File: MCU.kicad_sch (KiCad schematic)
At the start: 28 parts, among them J3 ADC_EXT_SUPPLY, U2 LPC55S28JBD100

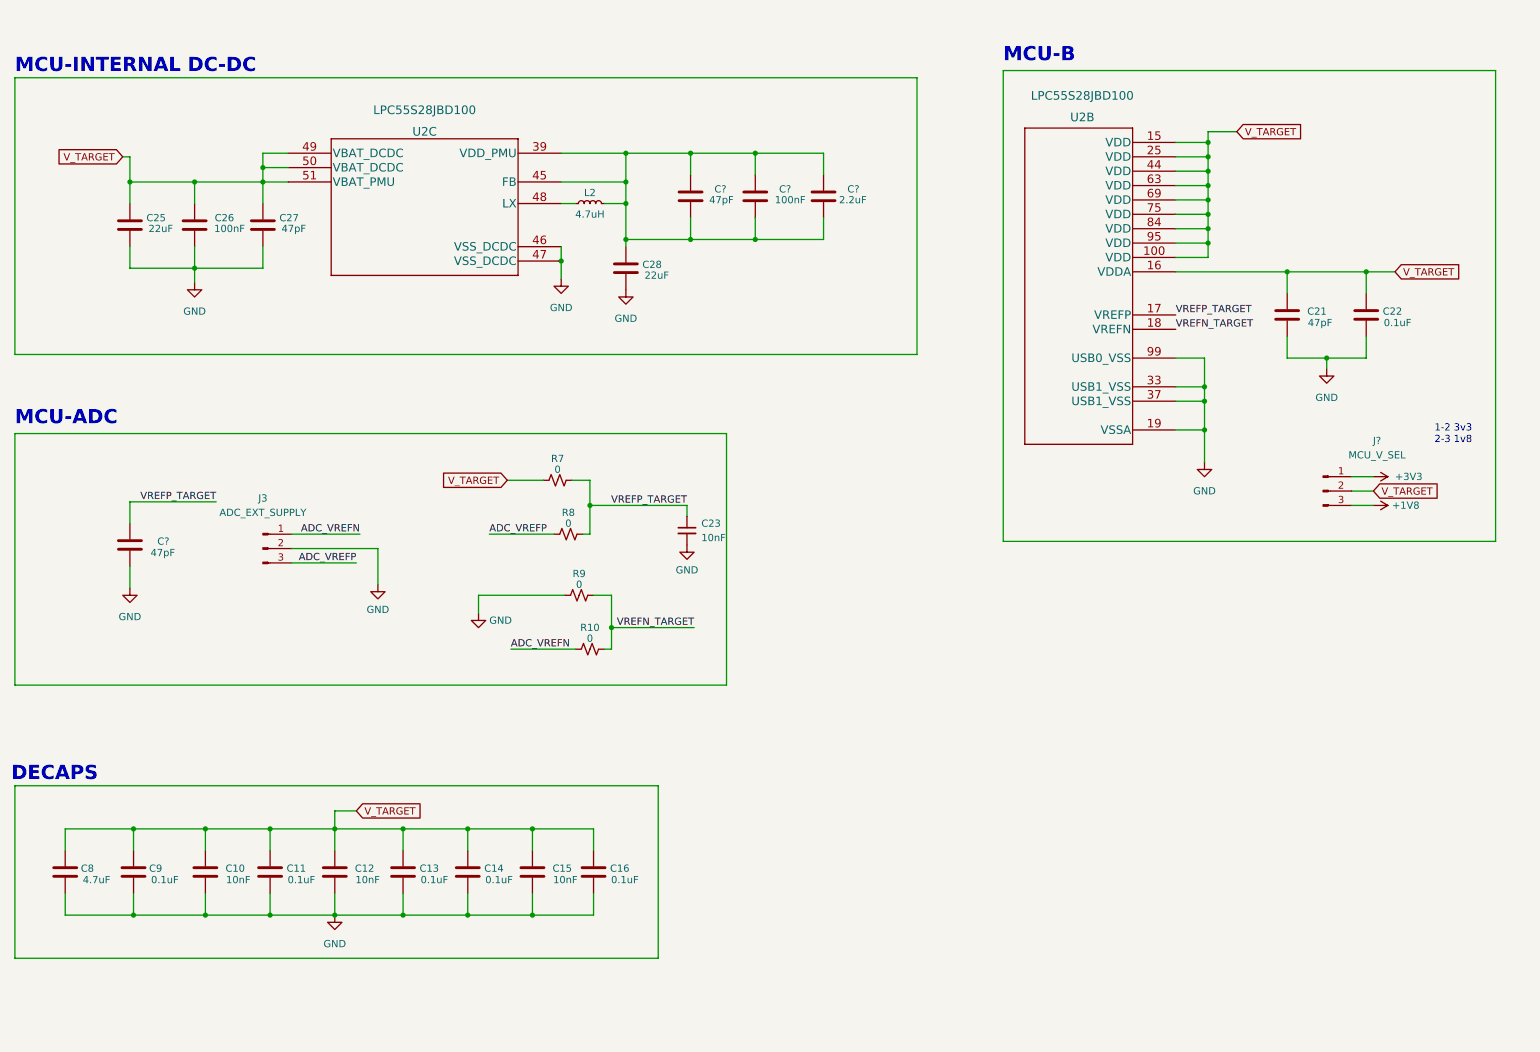
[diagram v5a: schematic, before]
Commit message: ISP Boot eklenecek
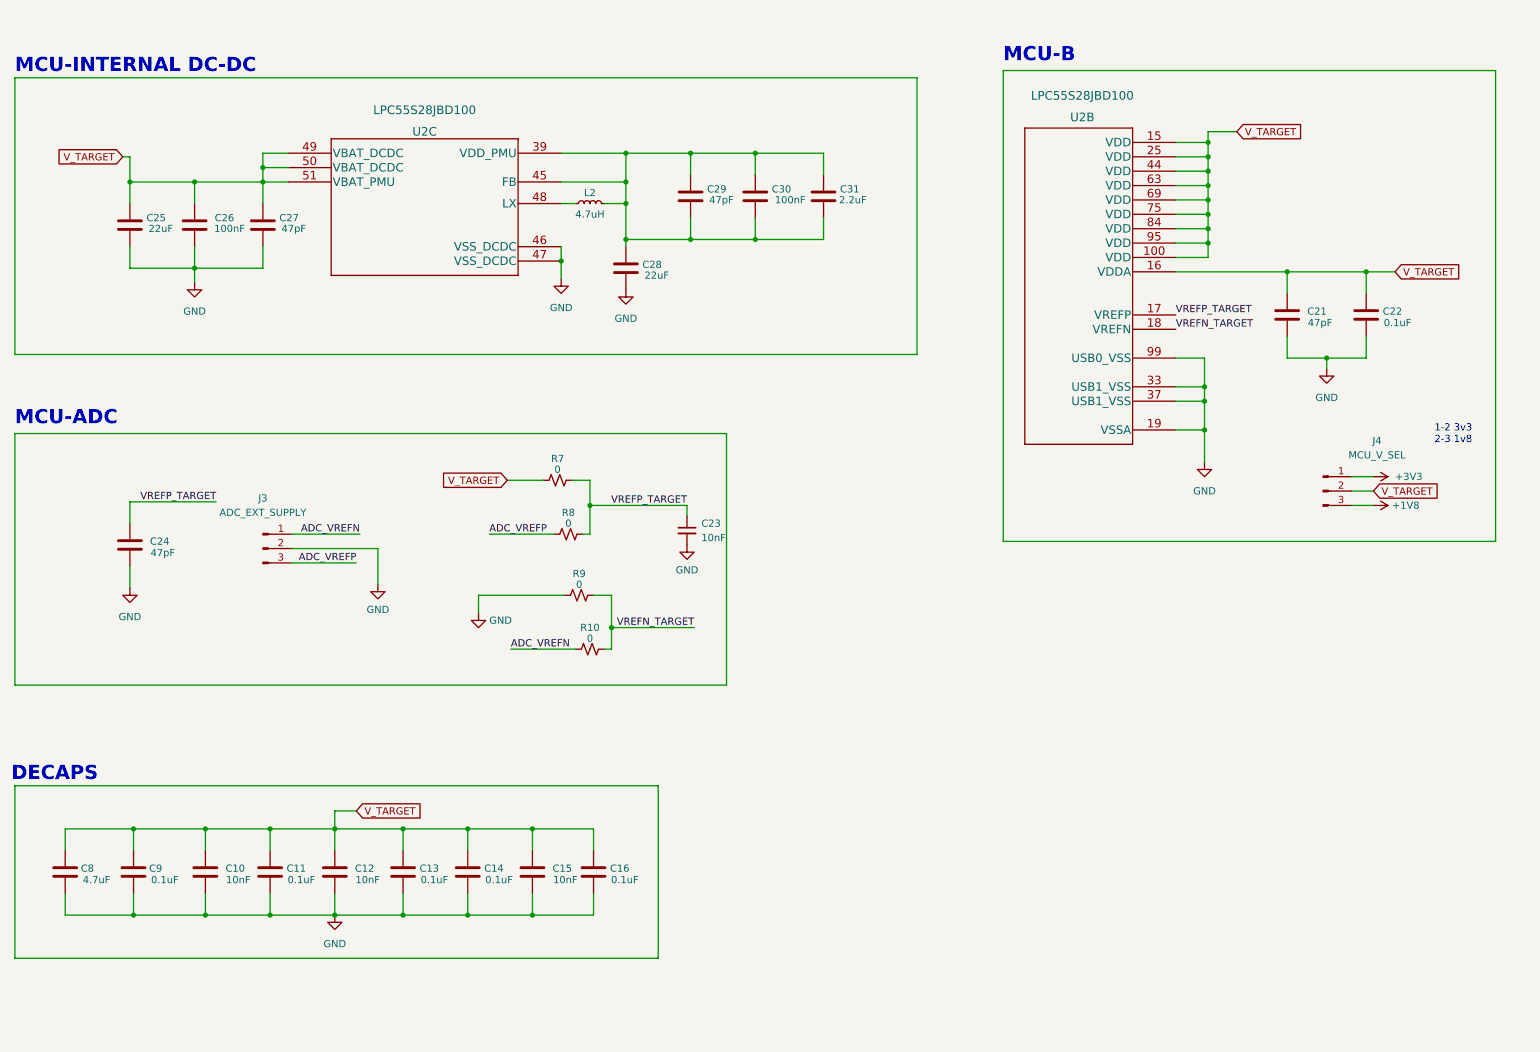
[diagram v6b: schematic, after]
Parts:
- C10, C11, C12, C13, C14, C15, C16, C21, C22, C25, C26, C27, C28, C8, C9: footprint Resistor_SMD:R_0603_1608Metric -> Capacitor_SMD:C_0603_1608Metric
- C23: footprint (none) -> Capacitor_SMD:C_0603_1608Metric
- C29, C30, C31: renamed from C?; footprint Resistor_SMD:R_0603_1608Metric -> Capacitor_SMD:C_0603_1608Metric
- U2: footprint HLQFP100 -> erkan-hw-lib:HLQFP100
- gave numbers to parts that had none: 2
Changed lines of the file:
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@@
       (effects (font (size 1.27 1.27)) (justify right))
     )
-    (property "Footprint" "Resistor_SMD:R_0603_1608Metric" (id 2) (at 78.4352 170.18 0)
+    (property "Footprint" "Capacitor_SMD:C_0603_1608Metric" (id 2) (at 78.4352 170.18 0)
       (effects (font (size 1.27 1.27)) hide)
     )
@@
       (effects (font (size 1.524 1.524)))
     )
-    (property "Footprint" "HLQFP100" (id 2) (at 122.555 30.734 0)
+    (property "Footprint" "erkan-hw-lib:HLQFP100" (id 2) (at 122.555 30.734 0)
       (effects (font (size 1.524 1.524)) hide)
     )
@@
   (symbol (lib_id "power:+1V8") (at 260.985 101.6 270) (unit 1)
     (in_bom yes) (on_board yes)
-    (property "Reference" "#PWR?" (id 0) (at 257.175 101.6 0)
+    (property "Reference" "#PWR0120" (id 0) (at 257.175 101.6 0)
       (effects (font (size 1.27 1.27)) hide)
     )
@@
       (effects (font (size 1.27 1.27)) (justify left))
     )
-    (property "Footprint" "" (id 2) (at 139.7 106.045 0)
+    (property "Footprint" "Capacitor_SMD:C_0603_1608Metric" (id 2) (at 139.7 106.045 0)
       (effects (font (size 1.27 1.27)) hide)
     )
@@
   (symbol (lib_id "Device:C") (at 163.83 46.99 0) (unit 1)
     (in_bom yes) (on_board yes)
-    (property "Reference" "C?" (id 0) (at 170.18 45.72 0)
+    (property "Reference" "C31" (id 0) (at 170.18 45.72 0)
       (effects (font (size 1.27 1.27)) (justify right))
     )
@@
       (effects (font (size 1.27 1.27)) (justify right))
     )
-    (property "Footprint" "Resistor_SMD:R_0603_1608Metric" (id 2) (at 164.7952 50.8 0)
+    (property "Footprint" "Capacitor_SMD:C_0603_1608Metric" (id 2) (at 164.7952 50.8 0)
       (effects (font (size 1.27 1.27)) hide)
     )
@@
   (symbol (lib_id "power:+3V3") (at 260.985 96.52 270) (unit 1)
     (in_bom yes) (on_board yes) (fields_autoplaced)
-    (property "Reference" "#PWR?" (id 0) (at 257.175 96.52 0)
+    (property "Reference" "#PWR0133" (id 0) (at 257.175 96.52 0)
       (effects (font (size 1.27 1.27)) hide)
     )
@@
   (symbol (lib_id "power:GND") (at 41.275 116.205 0) (unit 1)
     (in_bom yes) (on_board yes) (fields_autoplaced)
-    (property "Reference" "#PWR?" (id 0) (at 41.275 122.555 0)
+    (property "Reference" "#PWR0134" (id 0) (at 41.275 122.555 0)
       (effects (font (size 1.27 1.27)) hide)
     )
@@
       (effects (font (size 1.27 1.27)) (justify right))
     )
-    (property "Footprint" "Resistor_SMD:R_0603_1608Metric" (id 2) (at 42.8752 170.18 0)
+    (property "Footprint" "Capacitor_SMD:C_0603_1608Metric" (id 2) (at 42.8752 170.18 0)
       (effects (font (size 1.27 1.27)) hide)
     )
@@
   (symbol (lib_id "Device:C") (at 151.765 46.99 0) (unit 1)
     (in_bom yes) (on_board yes)
-    (property "Reference" "C?" (id 0) (at 158.115 45.72 0)
+    (property "Reference" "C30" (id 0) (at 158.115 45.72 0)
       (effects (font (size 1.27 1.27)) (justify right))
     )
@@
       (effects (font (size 1.27 1.27)) (justify right))
     )
-    (property "Footprint" "Resistor_SMD:R_0603_1608Metric" (id 2) (at 152.7302 50.8 0)
+    (property "Footprint" "Capacitor_SMD:C_0603_1608Metric" (id 2) (at 152.7302 50.8 0)
       (effects (font (size 1.27 1.27)) hide)
     )
@@
       (effects (font (size 1.27 1.27)) (justify right))
     )
-    (property "Footprint" "Resistor_SMD:R_0603_1608Metric" (id 2) (at 90.5002 170.18 0)
+    (property "Footprint" "Capacitor_SMD:C_0603_1608Metric" (id 2) (at 90.5002 170.18 0)
       (effects (font (size 1.27 1.27)) hide)
     )
@@
   (symbol (lib_id "Connector:Conn_01x03_Male") (at 252.095 99.06 0) (unit 1)
     (in_bom yes) (on_board yes)
-    (property "Reference" "J?" (id 0) (at 261.62 90.17 0))
+    (property "Reference" "J4" (id 0) (at 261.62 90.17 0))
     (property "Value" "MCU_V_SEL" (id 1) (at 261.62 92.71 0))
     (property "Footprint" "Connector_PinHeader_2.54mm:PinHeader_1x03_P2.54mm_Vertical" (id 2) (at 252.095 99.06 0)
@@
       (effects (font (size 1.27 1.27)) (justify right))
     )
-    (property "Footprint" "Resistor_SMD:R_0603_1608Metric" (id 2) (at 129.8702 63.5 0)
+    (property "Footprint" "Capacitor_SMD:C_0603_1608Metric" (id 2) (at 129.8702 63.5 0)
       (effects (font (size 1.27 1.27)) hide)
     )
@@
       (effects (font (size 1.27 1.27)) (justify right))
     )
-    (property "Footprint" "Resistor_SMD:R_0603_1608Metric" (id 2) (at 42.2402 55.88 0)
+    (property "Footprint" "Capacitor_SMD:C_0603_1608Metric" (id 2) (at 42.2402 55.88 0)
       (effects (font (size 1.27 1.27)) hide)
     )
@@
       (effects (font (size 1.27 1.27)) (justify right))
     )
-    (property "Footprint" "Resistor_SMD:R_0603_1608Metric" (id 2) (at 65.7352 55.88 0)
+    (property "Footprint" "Capacitor_SMD:C_0603_1608Metric" (id 2) (at 65.7352 55.88 0)
       (effects (font (size 1.27 1.27)) hide)
     )
@@
   (symbol (lib_id "Device:C") (at 140.335 46.99 0) (unit 1)
     (in_bom yes) (on_board yes)
-    (property "Reference" "C?" (id 0) (at 146.685 45.72 0)
+    (property "Reference" "C29" (id 0) (at 146.685 45.72 0)
       (effects (font (size 1.27 1.27)) (justify right))
     )
@@
       (effects (font (size 1.27 1.27)) (justify right))
     )
-    (property "Footprint" "Resistor_SMD:R_0603_1608Metric" (id 2) (at 141.3002 50.8 0)
+    (property "Footprint" "Capacitor_SMD:C_0603_1608Metric" (id 2) (at 141.3002 50.8 0)
       (effects (font (size 1.27 1.27)) hide)
     )
@@
       (effects (font (size 1.27 1.27)) (justify right))
     )
-    (property "Footprint" "Resistor_SMD:R_0603_1608Metric" (id 2) (at 246.7102 71.755 0)
+    (property "Footprint" "Capacitor_SMD:C_0603_1608Metric" (id 2) (at 246.7102 71.755 0)
       (effects (font (size 1.27 1.27)) hide)
     )
@@
       (effects (font (size 1.27 1.27)) (justify right))
     )
-    (property "Footprint" "Resistor_SMD:R_0603_1608Metric" (id 2) (at 260.6802 71.755 0)
+    (property "Footprint" "Capacitor_SMD:C_0603_1608Metric" (id 2) (at 260.6802 71.755 0)
       (effects (font (size 1.27 1.27)) hide)
     )
@@
       (effects (font (size 1.27 1.27)) (justify right))
     )
-    (property "Footprint" "Resistor_SMD:R_0603_1608Metric" (id 2) (at 30.8102 170.18 0)
+    (property "Footprint" "Capacitor_SMD:C_0603_1608Metric" (id 2) (at 30.8102 170.18 0)
       (effects (font (size 1.27 1.27)) hide)
     )
@@
   (symbol (lib_id "Device:C") (at 41.275 108.585 0) (unit 1)
     (in_bom yes) (on_board no)
-    (property "Reference" "C?" (id 0) (at 48.26 107.95 0)
+    (property "Reference" "C24" (id 0) (at 48.26 107.95 0)
       (effects (font (size 1.27 1.27)) (justify right))
     )
@@
       (effects (font (size 1.27 1.27)) (justify right))
     )
-    (property "Footprint" "Resistor_SMD:R_0603_1608Metric" (id 2) (at 124.1552 170.18 0)
+    (property "Footprint" "Capacitor_SMD:C_0603_1608Metric" (id 2) (at 124.1552 170.18 0)
       (effects (font (size 1.27 1.27)) hide)
     )
@@
       (effects (font (size 1.27 1.27)) (justify right))
     )
-    (property "Footprint" "Resistor_SMD:R_0603_1608Metric" (id 2) (at 53.6702 55.88 0)
+    (property "Footprint" "Capacitor_SMD:C_0603_1608Metric" (id 2) (at 53.6702 55.88 0)
       (effects (font (size 1.27 1.27)) hide)
     )
@@
       (effects (font (size 1.27 1.27)) (justify right))
     )
-    (property "Footprint" "Resistor_SMD:R_0603_1608Metric" (id 2) (at 67.0052 170.18 0)
+    (property "Footprint" "Capacitor_SMD:C_0603_1608Metric" (id 2) (at 67.0052 170.18 0)
       (effects (font (size 1.27 1.27)) hide)
     )
@@
       (effects (font (size 1.27 1.27)) (justify right))
     )
-    (property "Footprint" "Resistor_SMD:R_0603_1608Metric" (id 2) (at 101.9302 170.18 0)
+    (property "Footprint" "Capacitor_SMD:C_0603_1608Metric" (id 2) (at 101.9302 170.18 0)
       (effects (font (size 1.27 1.27)) hide)
     )
@@
       (effects (font (size 1.27 1.27)) (justify right))
     )
-    (property "Footprint" "Resistor_SMD:R_0603_1608Metric" (id 2) (at 55.5752 170.18 0)
+    (property "Footprint" "Capacitor_SMD:C_0603_1608Metric" (id 2) (at 55.5752 170.18 0)
       (effects (font (size 1.27 1.27)) hide)
     )
@@
       (effects (font (size 1.27 1.27)) (justify right))
     )
-    (property "Footprint" "Resistor_SMD:R_0603_1608Metric" (id 2) (at 113.3602 170.18 0)
-      (effects (font (size 1.27 1.27)) hide)
-    )
+    (property "Footprint" "Capacitor_SMD:C_0603_1608Metric" (id 2) (at 113.3602 170.18 0)
+      (effects (font (size 1.27 1.27)) hide)
+    )

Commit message: Butonlar eklendi
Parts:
- U5: renamed from U2; footprint erkan-hw-lib:HLQFP100 -> HLQFP100
- renumbered C8 to C10, C25 to C11, C24 to C12, C9 to C13, C26 to C14, C10 to C15, C27 to C16, C11 to C17, C12 to C18, C13 to C19, C14 to C20, C15 to C21, C16 to C22, C28 to C23, C23 to C24, C29 to C25, C30 to C26, C31 to C27, C21 to C28, C22 to C29, J3 to J4, J4 to J5, U2 to U5
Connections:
- net GND: now also U5.101 (EP)

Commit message: Pin labelları eklendi
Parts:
- U5: footprint HLQFP100 -> erkan-hw-lib:HLQFP100
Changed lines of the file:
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@@
       (effects (font (size 1.524 1.524)))
     )
-    (property "Footprint" "HLQFP100" (id 2) (at 180.34 31.369 0)
+    (property "Footprint" "erkan-hw-lib:HLQFP100" (id 2) (at 180.34 31.369 0)
       (effects (font (size 1.524 1.524)) hide)
     )
